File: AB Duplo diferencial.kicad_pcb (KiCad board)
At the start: 2 copper layers, 41 parts, among them Q1 C945, Q10 13007, Q11 13007, Q2 C945, Q3 A733, Q4 A733, Q5 A733, Q6 C945, Q7 C945, Q8 TIP41, Q9 TIP42

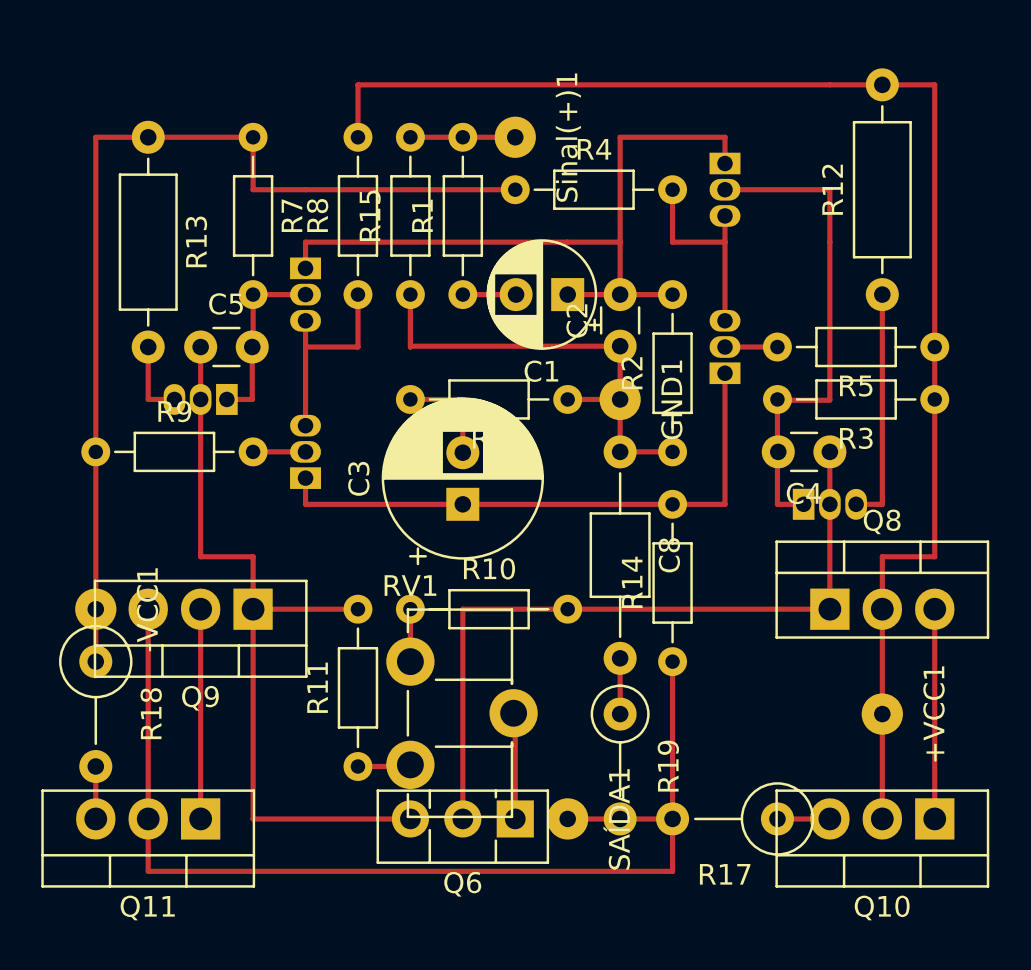
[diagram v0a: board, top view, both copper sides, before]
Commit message: [corrigido] TO-92_Inline pra TO-92_Inline_Wide & visão 3d no PcbView
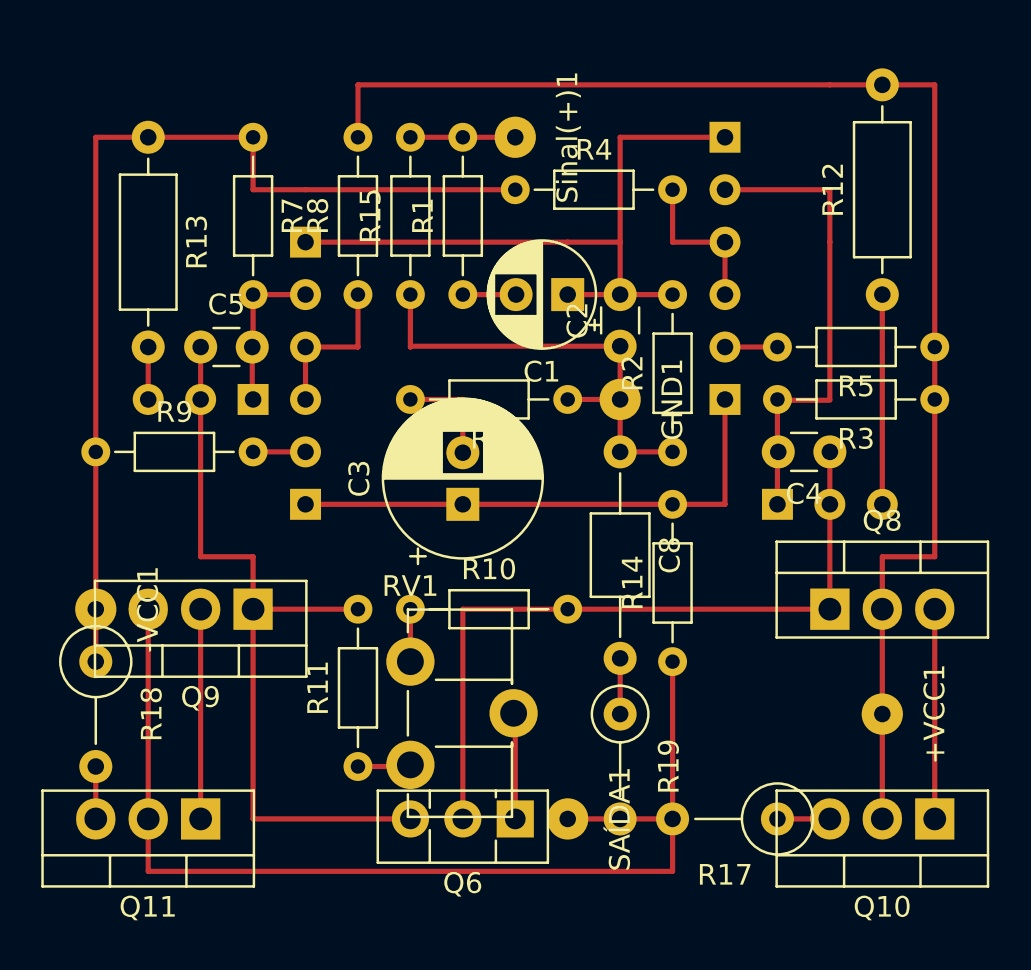
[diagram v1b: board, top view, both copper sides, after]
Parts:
- Q1, Q2, Q3, Q4, Q5, Q7: footprint Package_TO_SOT_THT:TO-92_Inline -> Package_TO_SOT_THT:TO-92_Inline_Wide
- moved Q2 1.27 mm to (96.5, 40.6)
- moved Q1 1.27 mm to (96.5, 27.9)
- moved Q3 1.27 mm to (76.2, 33.0)
- moved Q4 1.27 mm to (76.2, 45.7)
- moved Q5 1.27 mm to (99.1, 45.7)
- moved Q7 1.27 mm to (73.7, 40.6)
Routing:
- net Net-(Q3-Pad3): track 10.2 -> 7.62 mm
- net Net-(Q1-Pad3): track 10.2 -> 7.62 mm
- net Net-(C3-Pad1): track 27.9 -> 25.4 mm
- net Net-(C1-Pad1): track 35.6 -> 33.0 mm
- net Net-(Q7-Pad3): track 3.81 -> 2.54 mm
- net Net-(Q5-Pad3): track 11.4 -> 10.2 mm
- net Net-(C4-Pad2): track 24.1 -> 22.8 mm
- net Net-(C5-Pad2): track 8.87 -> 7.64 mm
